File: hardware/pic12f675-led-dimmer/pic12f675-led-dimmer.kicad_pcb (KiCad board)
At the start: 2 copper layers, 46 x 35 mm, 17 parts, among them J1 Conn_01x02_Pin, J2 Conn_01x02_Pin, J3 Conn_01x02_Pin, J4 Conn_01x02_Pin, J5 Conn_01x02_Pin, Q1 Q_NPN, Q2 Q_NPN, Q3 Q_NPN, Q4 Q_NPN, Q5 Q_NPN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

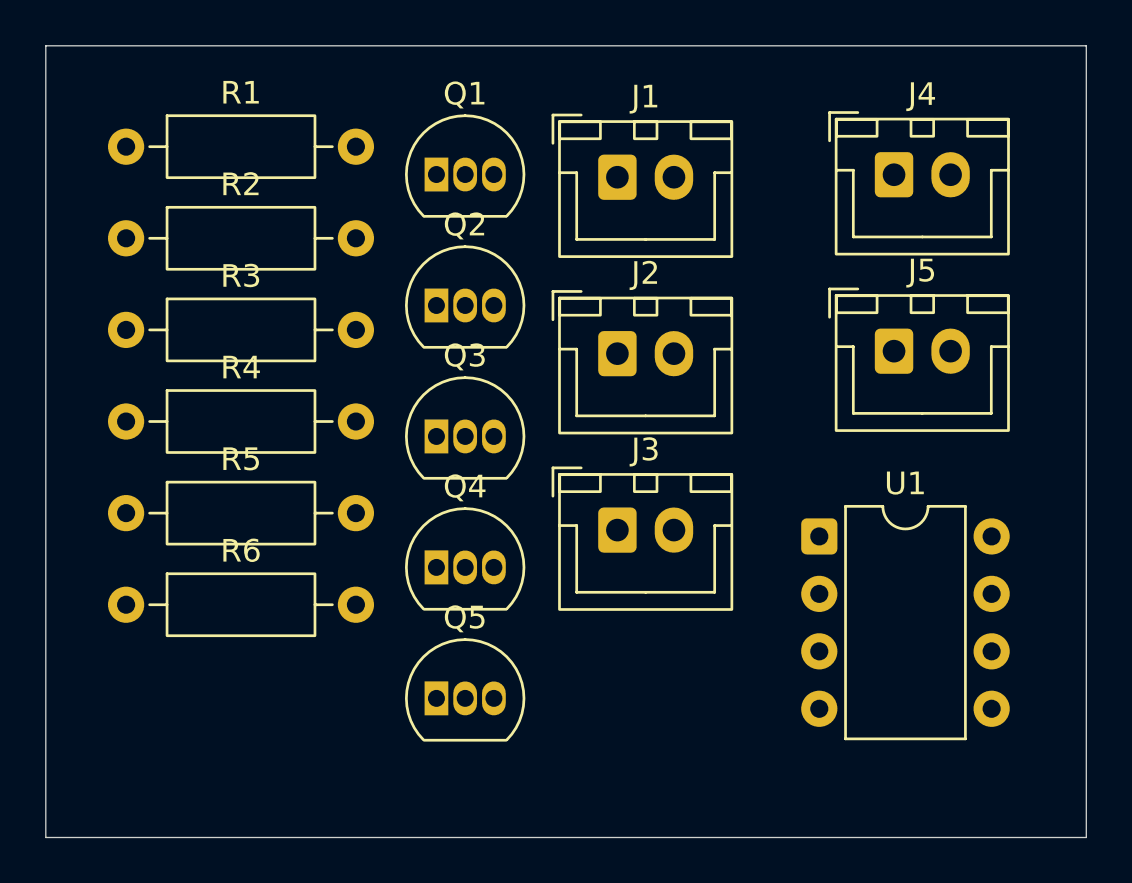
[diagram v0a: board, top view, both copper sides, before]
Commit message: refactor(hw): preparar espacio para integración de módulo buck step-down
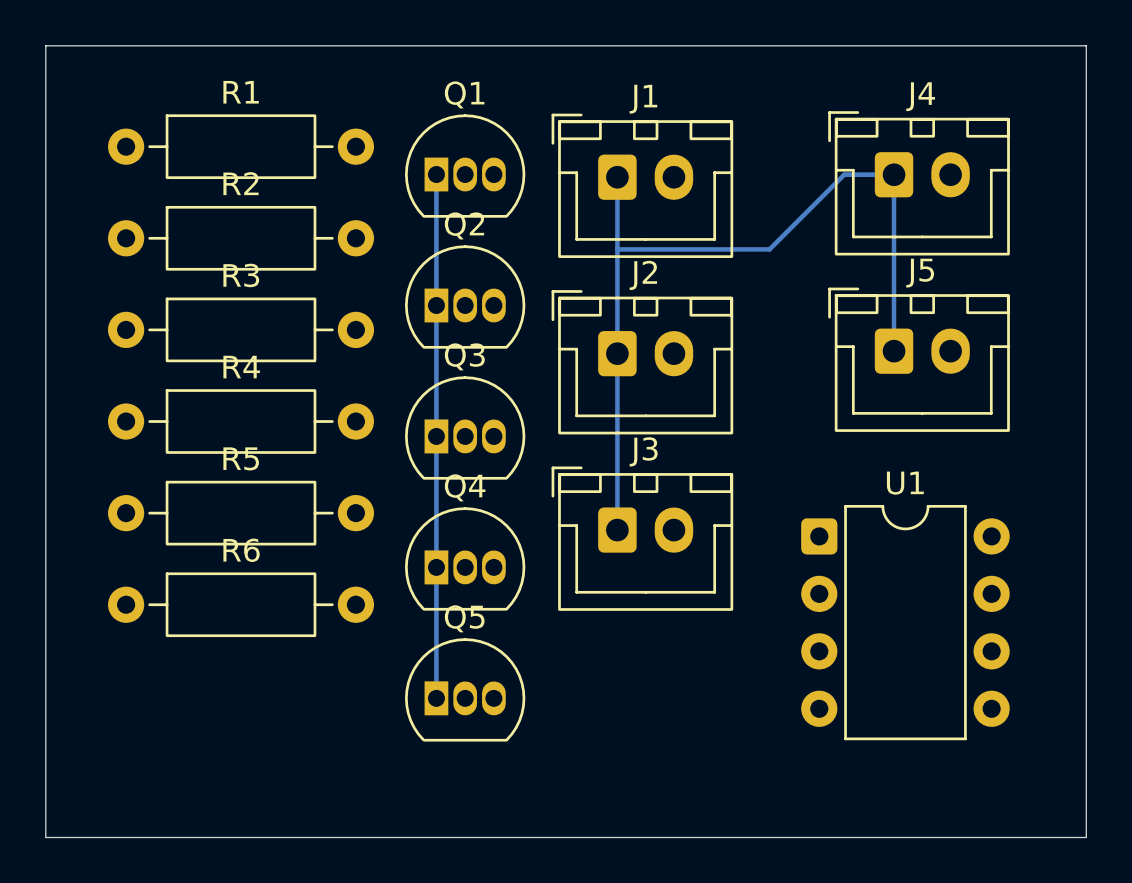
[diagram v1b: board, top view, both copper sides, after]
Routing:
- net +12V: track 0.00 -> 37.0 mm
- net (no net): track 0.00 -> 23.2 mm
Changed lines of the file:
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@@
 	(net 0 "")
 	(net 1 "+12V")
-	(net 2 "Net-(J1-Pin_2)")
+	(net 2 "Net-(D4-K)")
 	(net 3 "Net-(J2-Pin_2)")
 	(net 4 "Net-(J3-Pin_2)")
@@
 			(layers "*.Cu" "*.Mask")
 			(remove_unused_layers no)
-			(net 2 "Net-(J1-Pin_2)")
+			(net 2 "Net-(D4-K)")
 			(pinfunction "Pin_2")
 			(pintype "passive")
@@
 		(layer "Edge.Cuts")
 	)
+	(segment
+		(start 114.77 75.48)
+		(end 114.77 81.27)
+		(width 0.2)
+		(layer "B.Cu")
+		(net 0)
+	)
+	(segment
+		(start 114.77 69.69)
+		(end 114.77 75.48)
+		(width 0.2)
+		(layer "B.Cu")
+		(net 0)
+	)
+	(segment
+		(start 114.77 87.06)
+		(end 114.77 92.85)
+		(width 0.2)
+		(layer "B.Cu")
+		(net 0)
+	)
+	(segment
+		(start 114.77 81.27)
+		(end 114.77 87.06)
+		(width 0.2)
+		(layer "B.Cu")
+		(net 0)
+	)
+	(segment
+		(start 135 69.7)
+		(end 135 77.5)
+		(width 0.2)
+		(layer "B.Cu")
+		(net 1)
+	)
+	(segment
+		(start 129.5 73)
+		(end 122.77 73)
+		(width 0.2)
+		(layer "B.Cu")
+		(net 1)
+	)
+	(segment
+		(start 122.77 77.61)
+		(end 122.77 85.41)
+		(width 0.2)
+		(layer "B.Cu")
+		(net 1)
+	)
+	(segment
+		(start 135 69.7)
+		(end 132.8 69.7)
+		(width 0.2)
+		(layer "B.Cu")
+		(net 1)
+	)
+	(segment
+		(start 122.77 73)
+		(end 122.77 77.61)
+		(width 0.2)
+		(layer "B.Cu")
+		(net 1)
+	)
+	(segment
+		(start 132.8 69.7)
+		(end 129.5 73)
+		(width 0.2)
+		(layer "B.Cu")
+		(net 1)
+	)
+	(segment
+		(start 122.77 69.81)
+		(end 122.77 73)
+		(width 0.2)
+		(layer "B.Cu")
+		(net 1)
+	)
 	(embedded_fonts no)
